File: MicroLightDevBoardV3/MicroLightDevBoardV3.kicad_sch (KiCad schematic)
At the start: 23 parts, among them J1 TYPE-C-31-M-12, SW1 SW_Push, U1 STM32C071GBUx, U2 S-85S1AB33-I6T1U, U4 BQ25180, U5 USBLC6-2P6

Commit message: added button and integrated into pcb
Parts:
- C1, C2, C3: footprint Capacitor_SMD:C_0805_2012Metric -> Capacitor_SMD:C_0603_1608Metric
- SW1: footprint (none) -> MicroLightDevBoard:TS-1089S-02526
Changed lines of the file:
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@@
 			)
 		)
-		(property "Footprint" "Capacitor_SMD:C_0805_2012Metric"
+		(property "Footprint" "Capacitor_SMD:C_0603_1608Metric"
 			(at 173.6852 101.6 0)
 			(effects
@@
 			)
 		)
-		(property "Footprint" ""
+		(property "Footprint" "MicroLightDevBoard:TS-1089S-02526"
 			(at 113.03 167.64 0)
 			(effects
@@
 			)
 		)
-		(property "Footprint" "Capacitor_SMD:C_0805_2012Metric"
+		(property "Footprint" "Capacitor_SMD:C_0603_1608Metric"
 			(at 192.7352 106.68 0)
 			(effects
@@
 			)
 		)
-		(property "Footprint" "Capacitor_SMD:C_0805_2012Metric"
+		(property "Footprint" "Capacitor_SMD:C_0603_1608Metric"
 			(at 131.7752 101.6 0)
 			(effects

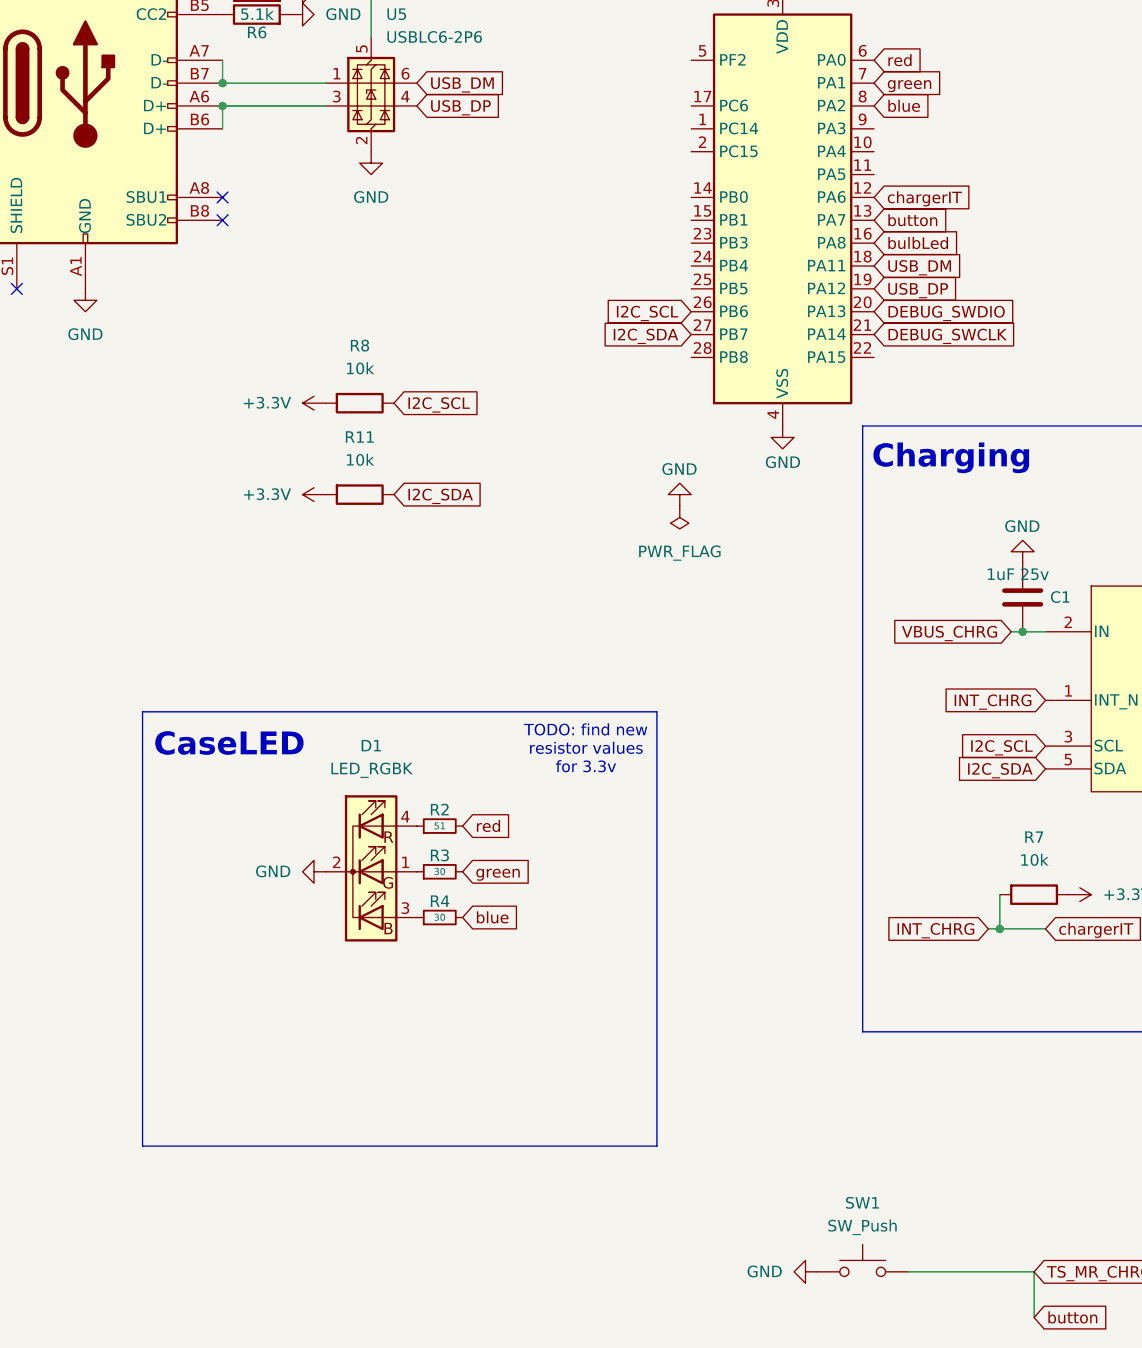
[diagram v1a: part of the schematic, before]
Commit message: move bulb led pin, work on pcb
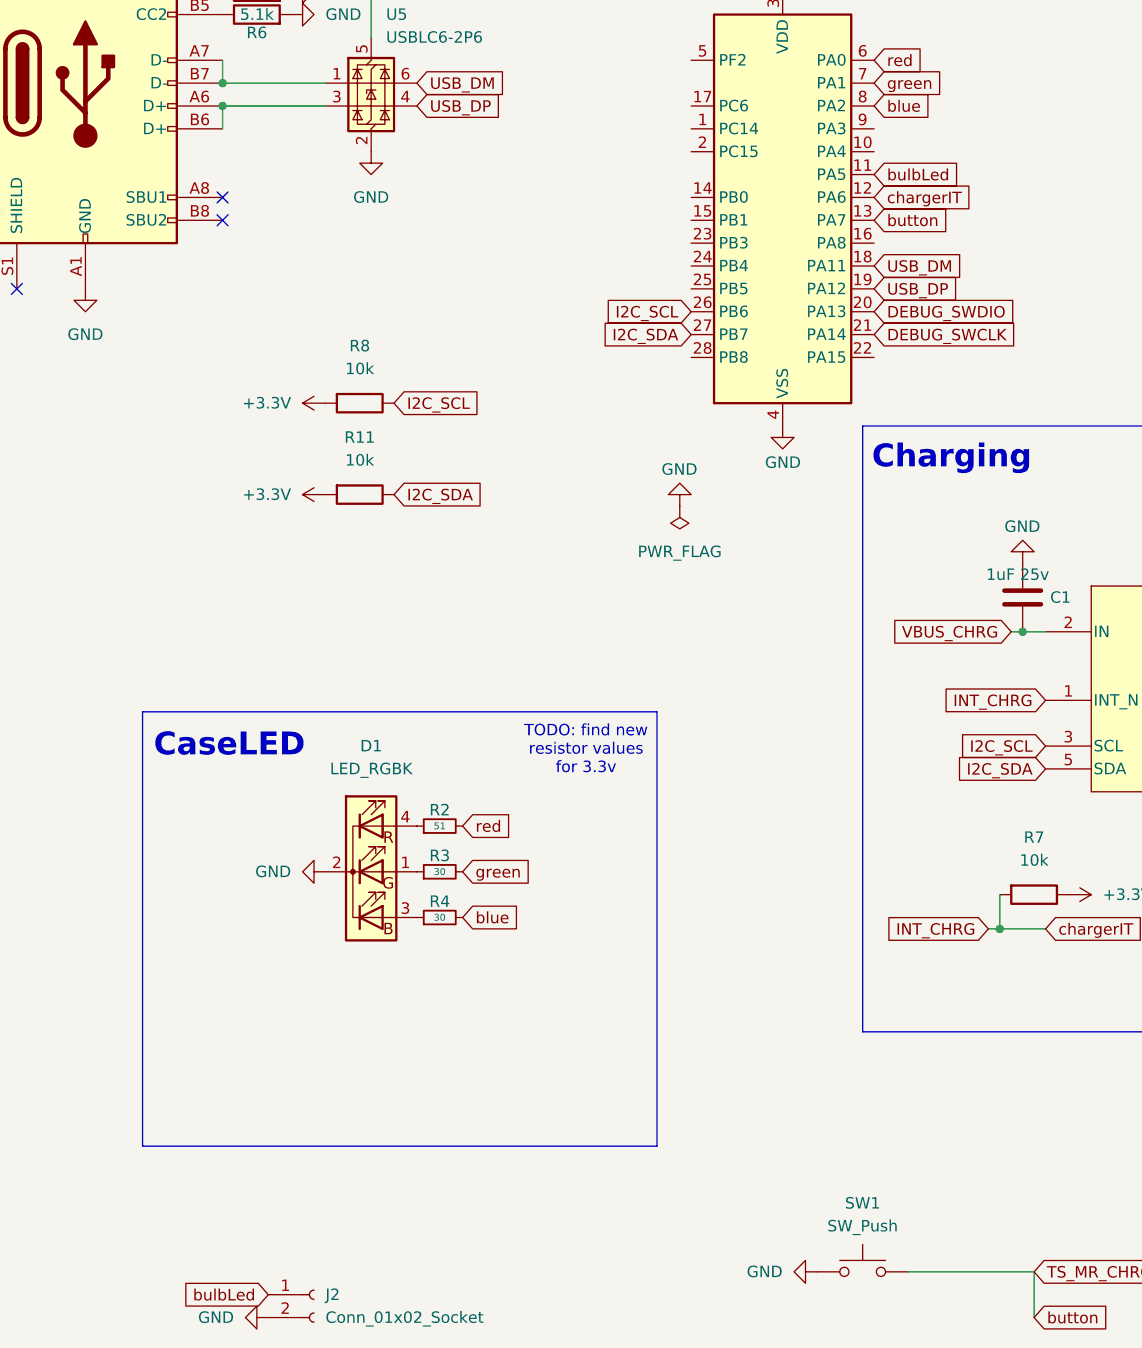
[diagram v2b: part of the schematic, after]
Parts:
- added J2: Conn_01x02_Socket, Connector_PinSocket_2.54mm:PinSocket_2x01_P2.54mm_Vertical, symbol Connector:Conn_01x02_Socket
- C1, C2, C3, C4, C5, C6, C7: footprint Capacitor_SMD:C_0603_1608Metric -> Capacitor_SMD:C_0402_1005Metric
- R11, R2, R3, R4, R5, R6, R7, R8: footprint Resistor_SMD:R_0603_1608Metric -> Resistor_SMD:R_0402_1005Metric
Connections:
- net GND: now also J2.2 (Pin_2)
- net bulbLed: now also U1.11 (PA5), J2.1 (Pin_1); no longer U1.16 (PA8)
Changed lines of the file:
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@@
 		)
 	)
-	(global_label "button"
+	(global_label "bulbLed"
 		(shape input)
-		(at 114.3 55.88 0)
+		(at 46.99 175.26 180)
 		(fields_autoplaced yes)
 		(effects
@@
 				(size 1.27 1.27)
 			)
-			(justify left)
+			(justify right)
 		)
 		(property "Intersheetrefs" "${INTERSHEET_REFS}"
-			(at 123.3326 55.88 0)
+			(at 36.6269 175.26 0)
 			(effects
 				(font
 					(size 1.27 1.27)
 				)
-				(justify left)
+				(justify right)
 				(hide yes)
 			)
 		)
 	)
-	(global_label "bulbLed"
+	(global_label "button"
 		(shape input)
-		(at 114.3 58.42 0)
+		(at 114.3 55.88 0)
 		(fields_autoplaced yes)
 		(effects
@@
 		)
 		(property "Intersheetrefs" "${INTERSHEET_REFS}"
-			(at 124.6631 58.42 0)
+			(at 123.3326 55.88 0)
 			(effects
 				(font
@@
 		)
 	)
+	(global_label "bulbLed"
+		(shape input)
+		(at 114.3 50.8 0)
+		(fields_autoplaced yes)
+		(effects
+			(font
+				(size 1.27 1.27)
+			)
+			(justify left)
+		)
+		(property "Intersheetrefs" "${INTERSHEET_REFS}"
+			(at 124.6631 50.8 0)
+			(effects
+				(font
+					(size 1.27 1.27)
+				)
+				(justify left)
+				(hide yes)
+			)
+		)
+	)
 	(symbol
 		(lib_id "power:GND")
@@
 			)
 		)
-		(property "Footprint" "Capacitor_SMD:C_0603_1608Metric"
+		(property "Footprint" "Capacitor_SMD:C_0402_1005Metric"
 			(at 173.6852 101.6 0)
 			(effects
@@
 			)
 		)
-		(property "Footprint" "Capacitor_SMD:C_0603_1608Metric"
+		(property "Footprint" "Capacitor_SMD:C_0402_1005Metric"
 			(at 93.98 22.5552 0)
 			(effects
@@
 			)
 		)
-		(property "Footprint" "Resistor_SMD:R_0603_1608Metric"
+		(property "Footprint" "Resistor_SMD:R_0402_1005Metric"
 			(at 132.08 129.032 90)
 			(effects
@@
 			)
 		)
-		(property "Footprint" "Resistor_SMD:R_0603_1608Metric"
+		(property "Footprint" "Resistor_SMD:R_0402_1005Metric"
 			(at 66.04 128.27 0)
 			(effects
@@
 			)
 		)
-		(property "Footprint" "Capacitor_SMD:C_0603_1608Metric"
+		(property "Footprint" "Capacitor_SMD:C_0402_1005Metric"
 			(at 93.98 27.6352 0)
 			(effects
@@
 			)
 		)
-		(property "Footprint" "Capacitor_SMD:C_0603_1608Metric"
+		(property "Footprint" "Capacitor_SMD:C_0402_1005Metric"
 			(at 192.7352 106.68 0)
 			(effects
@@
 			)
 		)
-		(property "Footprint" "Capacitor_SMD:C_0603_1608Metric"
+		(property "Footprint" "Capacitor_SMD:C_0402_1005Metric"
 			(at 160.9852 63.5 0)
 			(effects
@@
 			)
 		)
-		(property "Footprint" "Resistor_SMD:R_0603_1608Metric"
+		(property "Footprint" "Resistor_SMD:R_0402_1005Metric"
 			(at 66.04 133.35 0)
 			(effects
@@
 			)
 		)
-		(property "Footprint" "Capacitor_SMD:C_0603_1608Metric"
+		(property "Footprint" "Capacitor_SMD:C_0402_1005Metric"
 			(at 131.7752 101.6 0)
 			(effects
@@
 			)
 		)
-		(property "Footprint" "Resistor_SMD:R_0603_1608Metric"
+		(property "Footprint" "Resistor_SMD:R_0402_1005Metric"
 			(at 57.15 84.582 90)
 			(effects
@@
 			)
 		)
-		(property "Footprint" "Resistor_SMD:R_0603_1608Metric"
+		(property "Footprint" "Resistor_SMD:R_0402_1005Metric"
 			(at 57.15 74.422 90)
 			(effects
@@
 	(symbol
 		(lib_id "power:GND")
+		(at 46.99 177.8 270)
+		(unit 1)
+		(exclude_from_sim no)
+		(in_bom yes)
+		(on_board yes)
+		(dnp no)
+		(fields_autoplaced yes)
+		(property "Reference" "#PWR05"
+			(at 40.64 177.8 0)
+			(effects
+				(font
+					(size 1.27 1.27)
+				)
+				(hide yes)
+			)
+		)
+		(property "Value" "GND"
+			(at 43.18 177.7999 90)
+			(effects
+				(font
+					(size 1.27 1.27)
+				)
+				(justify right)
+			)
+		)
+		(property "Footprint" ""
+			(at 46.99 177.8 0)
+			(effects
+				(font
+					(size 1.27 1.27)
+				)
+				(hide yes)
+			)
+		)
+		(property "Datasheet" ""
+			(at 46.99 177.8 0)
+			(effects
+				(font
+					(size 1.27 1.27)
+				)
+				(hide yes)
+			)
+		)
+		(property "Description" "Power symbol creates a global label with name \"GND\" , ground"
+			(at 46.99 177.8 0)
+			(effects
+				(font
+					(size 1.27 1.27)
+				)
+				(hide yes)
+			)
+		)
+		(pin "1"
+		)
+		(instances
+			(project "MicroLightDevBoardV3"
+				(path "/9009d70b-273c-45fe-8624-596a22a35a49"
+					(reference "#PWR05")
+					(unit 1)
+				)
+			)
+		)
+	)
+	(symbol
+		(lib_id "power:GND")
 		(at 104.14 78.74 0)
 		(unit 1)
@@
 			)
 		)
-		(property "Footprint" "Capacitor_SMD:C_0603_1608Metric"
+		(property "Footprint" "Capacitor_SMD:C_0402_1005Metric"
 			(at 233.3752 66.04 0)
 			(effects
@@
 	)
 	(symbol
+		(lib_id "Connector:Conn_01x02_Socket")
+		(at 52.07 175.26 0)
+		(unit 1)
+		(exclude_from_sim no)
+		(in_bom yes)
+		(on_board yes)
+		(dnp no)
+		(fields_autoplaced yes)
+		(property "Reference" "J2"
+			(at 53.34 175.2599 0)
+			(effects
+				(font
+					(size 1.27 1.27)
+				)
+				(justify left)
+			)
+		)
+		(property "Value" "Conn_01x02_Socket"
+			(at 53.34 177.7999 0)
+			(effects
+				(font
+					(size 1.27 1.27)
+				)
+				(justify left)
+			)
+		)
+		(property "Footprint" "Connector_PinSocket_2.54mm:PinSocket_2x01_P2.54mm_Vertical"
+			(at 52.07 175.26 0)
+			(effects
+				(font
+					(size 1.27 1.27)
+				)
+				(hide yes)
+			)
+		)
+		(property "Datasheet" "~"
+			(at 52.07 175.26 0)
+			(effects
+				(font
+					(size 1.27 1.27)
+				)
+				(hide yes)
+			)
+		)
+		(property "Description" "Generic connector, single row, 01x02, script generated"
+			(at 52.07 175.26 0)
+			(effects
+				(font
+					(size 1.27 1.27)
+				)
+				(hide yes)
+			)
+		)
+		(pin "2"
+		)
+		(pin "1"
+		)
+		(instances
+			(project ""
+				(path "/9009d70b-273c-45fe-8624-596a22a35a49"
+					(reference "J2")
+					(unit 1)
+				)
+			)
+		)
+	)
+	(symbol
 		(lib_id "Device:R")
 		(at 45.72 30.48 90)
@@
 			)
 		)
-		(property "Footprint" "Resistor_SMD:R_0603_1608Metric"
+		(property "Footprint" "Resistor_SMD:R_0402_1005Metric"
 			(at 45.72 32.258 90)
 			(effects
@@
 			)
 		)
-		(property "Footprint" "Resistor_SMD:R_0603_1608Metric"
+		(property "Footprint" "Resistor_SMD:R_0402_1005Metric"
 			(at 45.72 34.798 90)
 			(effects
@@
 			)
 		)
-		(property "Footprint" "Resistor_SMD:R_0603_1608Metric"
+		(property "Footprint" "Resistor_SMD:R_0402_1005Metric"
 			(at 66.04 123.19 0)
 			(effects

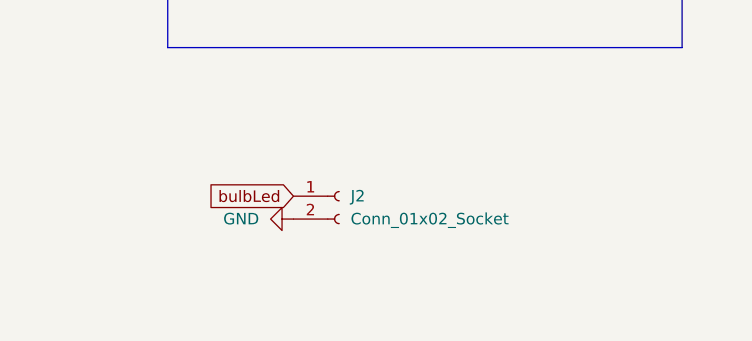
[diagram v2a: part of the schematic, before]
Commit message: added debug connector and mousebites to remove it
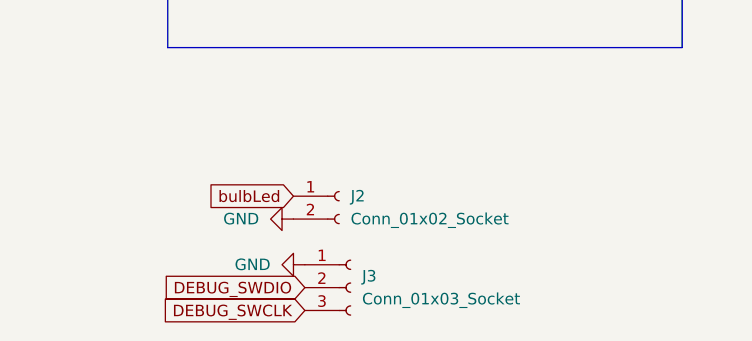
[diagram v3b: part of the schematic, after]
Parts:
- added J3: Conn_01x03_Socket, Connector_PinSocket_2.54mm:PinSocket_1x03_P2.54mm_Vertical, symbol Connector:Conn_01x03_Socket
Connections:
- net DEBUG_SWCLK: now also J3.3 (Pin_3)
- net DEBUG_SWDIO: now also J3.2 (Pin_2)
- net GND: now also J3.1 (Pin_1)
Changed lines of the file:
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@@
+		)
+	)
+	(global_label "DEBUG_SWCLK"
+		(shape input)
+		(at 48.26 187.96 180)
+		(fields_autoplaced yes)
+		(effects
+			(font
+				(size 1.27 1.27)
+			)
+			(justify right)
+		)
+		(property "Intersheetrefs" "${INTERSHEET_REFS}"
+			(at 31.7887 187.96 0)
+			(effects
+				(font
+					(size 1.27 1.27)
+				)
+				(justify right)
+				(hide yes)
+			)
 		)
 	)
@@
 		)
 	)
+	(global_label "DEBUG_SWDIO"
+		(shape input)
+		(at 48.26 185.42 180)
+		(fields_autoplaced yes)
+		(effects
+			(font
+				(size 1.27 1.27)
+			)
+			(justify right)
+		)
+		(property "Intersheetrefs" "${INTERSHEET_REFS}"
+			(at 32.1515 185.42 0)
+			(effects
+				(font
+					(size 1.27 1.27)
+				)
+				(justify right)
+				(hide yes)
+			)
+		)
+	)
 	(global_label "red"
 		(shape input)
@@
 	)
 	(symbol
+		(lib_id "power:GND")
+		(at 48.26 182.88 270)
+		(unit 1)
+		(exclude_from_sim no)
+		(in_bom yes)
+		(on_board yes)
+		(dnp no)
+		(fields_autoplaced yes)
+		(property "Reference" "#PWR013"
+			(at 41.91 182.88 0)
+			(effects
+				(font
+					(size 1.27 1.27)
+				)
+				(hide yes)
+			)
+		)
+		(property "Value" "GND"
+			(at 44.45 182.8799 90)
+			(effects
+				(font
+					(size 1.27 1.27)
+				)
+				(justify right)
+			)
+		)
+		(property "Footprint" ""
+			(at 48.26 182.88 0)
+			(effects
+				(font
+					(size 1.27 1.27)
+				)
+				(hide yes)
+			)
+		)
+		(property "Datasheet" ""
+			(at 48.26 182.88 0)
+			(effects
+				(font
+					(size 1.27 1.27)
+				)
+				(hide yes)
+			)
+		)
+		(property "Description" "Power symbol creates a global label with name \"GND\" , ground"
+			(at 48.26 182.88 0)
+			(effects
+				(font
+					(size 1.27 1.27)
+				)
+				(hide yes)
+			)
+		)
+		(pin "1"
+		)
+		(instances
+			(project "MicroLightDevBoardV3"
+				(path "/9009d70b-273c-45fe-8624-596a22a35a49"
+					(reference "#PWR013")
+					(unit 1)
+				)
+			)
+		)
+	)
+	(symbol
 		(lib_id "power:PWR_FLAG")
 		(at 92.71 87.63 180)
@@
 					(unit 1)
 				)
+			)
+		)
+	)
+	(symbol
+		(lib_id "Connector:Conn_01x03_Socket")
+		(at 53.34 185.42 0)
+		(unit 1)
+		(exclude_from_sim no)
+		(in_bom yes)
+		(on_board yes)
+		(dnp no)
+		(fields_autoplaced yes)
+		(property "Reference" "J3"
+			(at 54.61 184.1499 0)
+			(effects
+				(font
+					(size 1.27 1.27)
+				)
+				(justify left)
+			)
+		)
+		(property "Value" "Conn_01x03_Socket"
+			(at 54.61 186.6899 0)
+			(effects
+				(font
+					(size 1.27 1.27)
+				)
+				(justify left)
+			)
+		)
+		(property "Footprint" "Connector_PinSocket_2.54mm:PinSocket_1x03_P2.54mm_Vertical"
+			(at 53.34 185.42 0)
+			(effects
+				(font
+					(size 1.27 1.27)
+				)
+				(hide yes)
+			)
+		)
+		(property "Datasheet" "~"
+			(at 53.34 185.42 0)
+			(effects
+				(font
+					(size 1.27 1.27)
+				)
+				(hide yes)
+			)
+		)
+		(property "Description" "Generic connector, single row, 01x03, script generated"
+			(at 53.34 185.42 0)
+			(effects
+				(font
+					(size 1.27 1.27)
+				)
+				(hide yes)
+			)
+		)
+		(pin "2"
+		)
+		(pin "3"
+		)
+		(pin "1"
+		)
+		(instances
+			(project ""
+				(path "/9009d70b-273c-45fe-8624-596a22a35a49"
+					(reference "J3")
+					(unit 1)
+				)

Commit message: add jlcpcb part numbers
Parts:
- J1: LCSC (none) -> C165948
- U1: LSCS (none) -> C42240018
- U2: LSCS (none) -> C7070110
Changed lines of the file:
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@@
+			)
+		)
+		(property "LCSC" "C165948"
+			(at 26.67 41.91 0)
+			(effects
+				(font
+					(size 1.27 1.27)
+				)
+				(hide yes)
 			)
 		)
@@
 			)
 		)
+		(property "LSCS" "C7070110"
+			(at 186.69 55.88 0)
+			(effects
+				(font
+					(size 1.27 1.27)
+				)
+				(hide yes)
+			)
+		)
 		(pin "1"
 		)
@@
 			(at 104.14 55.88 0)
 			(effects
+				(font
+					(size 1.27 1.27)
+				)
+				(hide yes)
+			)
+		)
+		(property "LSCS" "C42240018"
+			(at 104.14 55.88 0)
+			(effects
